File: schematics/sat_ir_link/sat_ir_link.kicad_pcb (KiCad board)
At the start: 2 copper layers, 80 x 42.5 mm, 19 parts, among them J1 Conn_01x05, J2 TSOP38238, Q1 2N2222

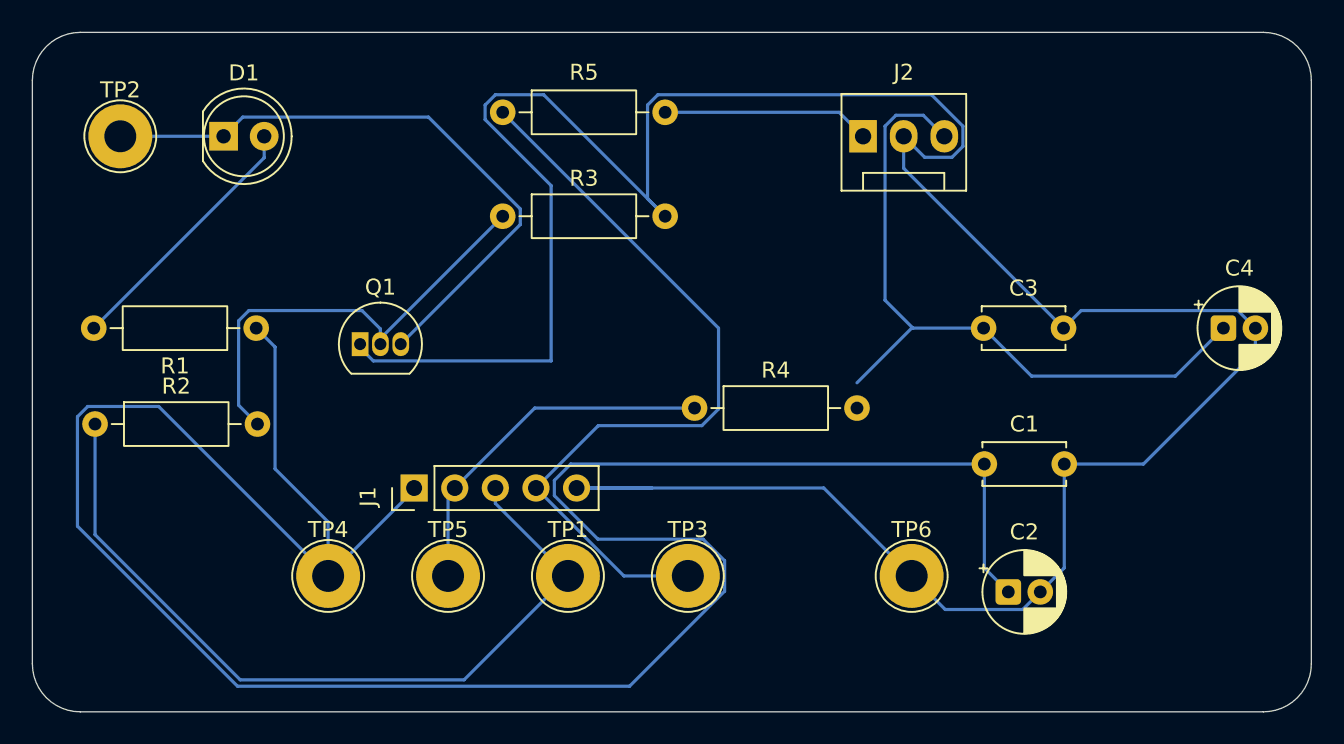
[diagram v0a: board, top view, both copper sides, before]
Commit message: feat(COMMS): 3d printed circuit file
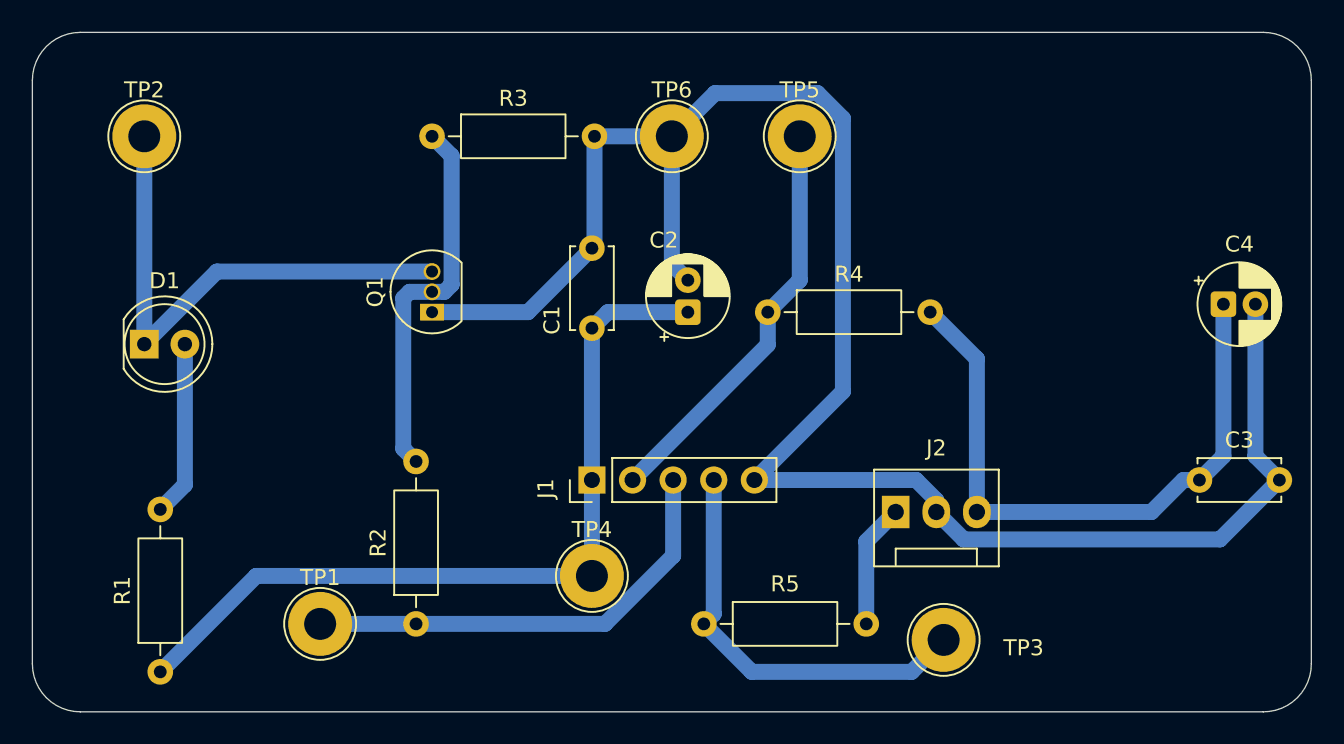
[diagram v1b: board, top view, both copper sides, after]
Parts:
- TP1: value TestPoint -> TX Test
- TP2: value TestPoint -> EDC Test
- TP3: value TestPoint -> RX Test
- TP4: value TestPoint -> 5v Test
- TP5: value TestPoint -> 3v3 Test
- TP6: value TestPoint -> GND Test
- moved TP5 35.2 mm to (153.0, 79.5)
- moved R5 34.4 mm to (147.0, 110.0)
- moved TP6 31.3 mm to (145.0, 79.5)
- moved C2 26.6 mm to (146.0, 90.5), turned to 90 degrees
- moved C1 26.0 mm to (140.0, 91.5), turned to 90 degrees
- moved R2 23.7 mm to (129.0, 110.0), turned to 90 degrees
- moved J2 23.6 mm to (159.0, 103.0)
- moved R1 22.3 mm to (113.0, 113.0), turned to 90 degrees
- moved C3 16.5 mm to (178.0, 101.0)
- moved TP4 16.5 mm to (140.0, 107.0)
- moved TP3 16.5 mm to (162.0, 111.0)
- moved TP1 15.8 mm to (123.0, 110.0)
- moved D1 13.9 mm to (112.0, 92.5)
- moved J1 11.1 mm to (140.0, 101.0)
- moved R4 7.55 mm to (151.0, 90.5)
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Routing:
- net /+5V: track 150.5 -> 51.4 mm
- net /GND: track 170.8 -> 118.3 mm
- net /RX_GPIO: track 49.4 -> 26.3 mm
- net /TX_GPIO: track 50.3 -> 28.6 mm
- net Net-(D1-K): track 39.5 -> 32.9 mm
- net Net-(J2-Pin_1): track 13.6 -> 7.76 mm
- net Net-(D1-A): track 16.4 -> 11.0 mm
- net Net-(Q1-B): track 28.8 -> 23.7 mm
- net /RX_3V3_FILTERED: track 44.7 -> 40.1 mm
- net /+3.3v: track 22.7 -> 25.8 mm

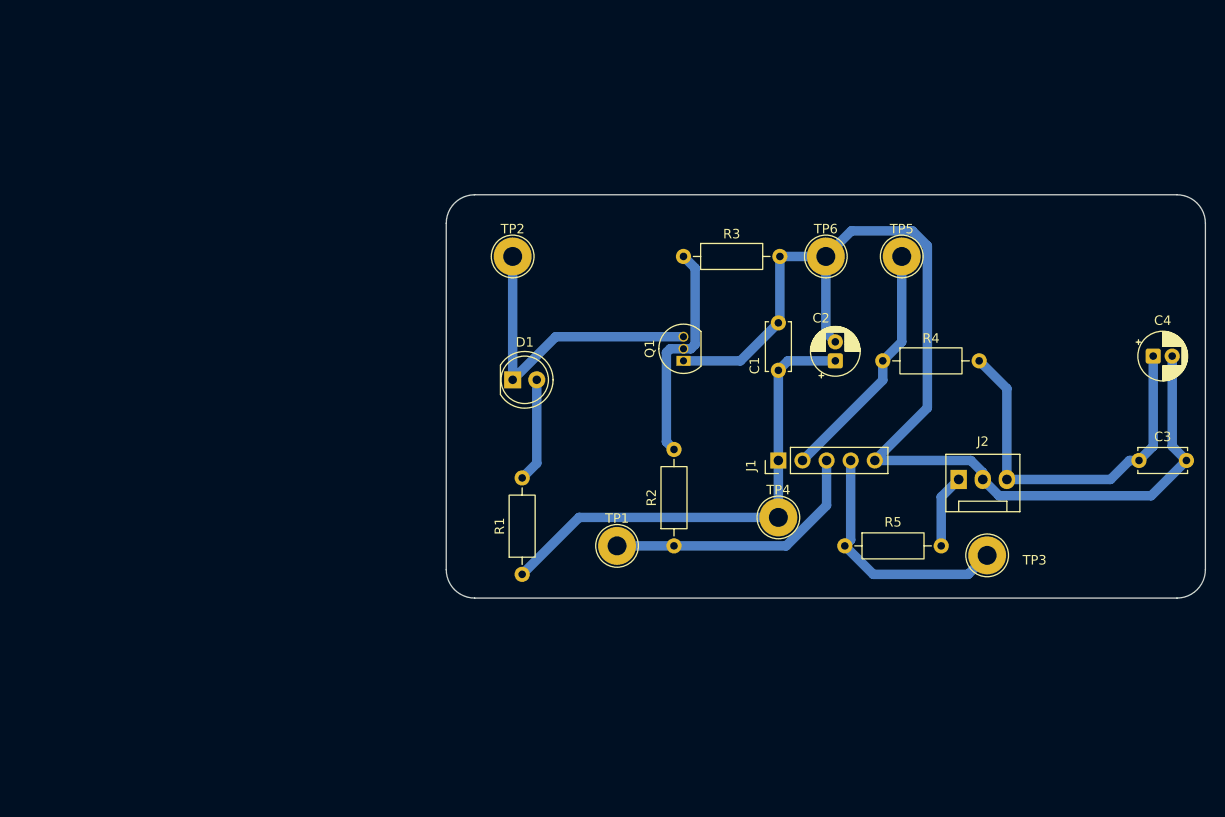
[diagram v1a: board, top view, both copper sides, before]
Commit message: New board circuits to fix design issues
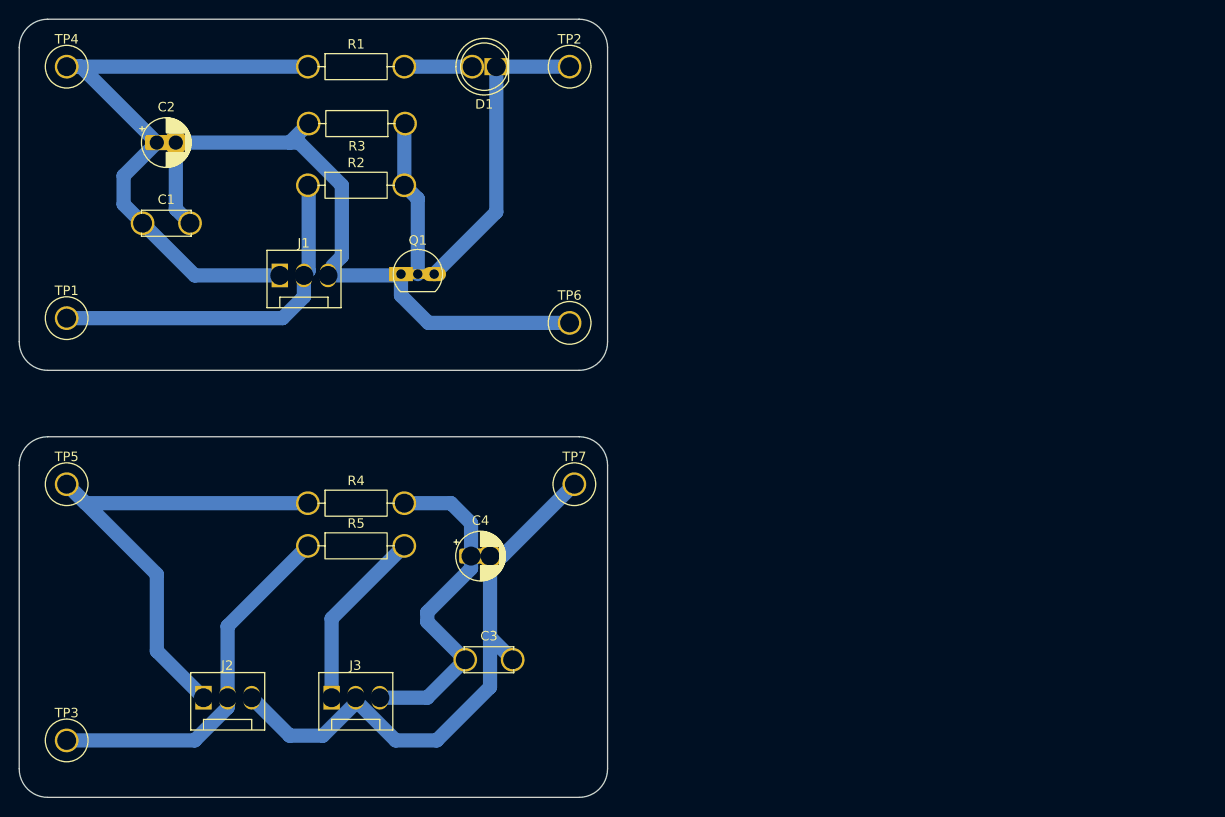
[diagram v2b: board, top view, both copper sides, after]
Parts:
- added J3: TSOP38238, Connector:FanPinHeader_1x03_P2.54mm_Vertical, F.Cu at (92.9, 126.0)
- added TP7: TestPoint, TestPoint:TestPoint_THTPad_D4.0mm_Drill2.0mm, F.Cu at (118.5, 103.5)
- J1: value Conn_01x05 -> TX Connector; footprint Connector_PinHeader_2.54mm:PinHeader_1x05_P2.54mm_Vertical -> Connector:FanPinHeader_1x03_P2.54mm_Vertical
- J2: value TSOP38238 -> RX Connector
- TP1: value TX Test -> TestPoint
- TP2: value EDC Test -> TestPoint
- TP3: value RX Test -> TestPoint
- TP4: value 5v Test -> TestPoint
- TP5: value 3v3 Test -> TestPoint
- TP6: value GND Test -> TestPoint
- moved TP3 98.9 mm to (65.0, 130.5)
- moved TP5 91.2 mm to (65.0, 103.5)
- moved TP4 88.8 mm to (65.0, 59.5)
- moved J2 82.8 mm to (79.4, 126.0)
- moved C2 75.1 mm to (74.5, 67.5), turned to 0 degrees
- moved C4 74.9 mm to (107.6, 111.1)
- moved C3 74.0 mm to (107.0, 122.0)
- moved C1 68.8 mm to (73.0, 76.0), turned to 0 degrees
- moved TP1 62.8 mm to (65.0, 86.0)
- moved R4 62.4 mm to (90.4, 105.5)
- moved R1 58.1 mm to (90.4, 59.5), turned to 0 degrees
- moved R5 56.6 mm to (90.4, 110.0)
- moved J1 56.0 mm to (87.5, 81.5), turned to 0 degrees
- moved R2 54.2 mm to (90.4, 72.0), turned to 0 degrees
- moved D1 33.0 mm to (110.3, 59.5), turned to 180 degrees
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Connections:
- C3 pad 2: /GND -> /GND2
- C4 pad 2: /GND -> /GND2
- J1 pad 2: /+3.3v -> /TX_GPIO
- J1 pad 3: /TX_GPIO -> /GND
- J2 pad 1: Net-(J2-Pin_1) -> /+3.3v
- J2 pad 2: /GND -> /RX_GPIO
- J2 pad 3: /RX_3V3_FILTERED -> /GND2
- R5 pad 2: Net-(J2-Pin_1) -> Net-(J3-Pin_1)
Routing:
- net /GND2: track 0.00 -> 62.3 mm
- net /GND: track 118.3 -> 69.2 mm
- net /+3.3v: track 25.8 -> 54.7 mm
- net Net-(J3-Pin_1): track 0.00 -> 19.2 mm
- net /+5V: track 51.4 -> 65.8 mm
- net /RX_GPIO: track 26.3 -> 38.9 mm
- net /TX_GPIO: track 28.6 -> 37.9 mm
- net Net-(J2-Pin_1): track 7.76 -> 0.00 mm
- net Net-(Q1-B): track 23.7 -> 16.5 mm
- net Net-(D1-A): track 11.0 -> 7.16 mm
- net /RX_3V3_FILTERED: track 40.1 -> 36.5 mm
- net Net-(D1-K): track 32.9 -> 32.3 mm
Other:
- board size 80 x 42.5 mm -> 62 x 82 mm
